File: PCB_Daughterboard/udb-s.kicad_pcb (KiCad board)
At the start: 4 copper layers, 50 x 20 mm, 10 parts, among them J1 TYPE-C-31-M-12, J2 78171-0004, U1 TPD4E05U06DQAR

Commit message: Update daughterboard 3d model
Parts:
- J2: value 78171-0004 -> 200528-0040
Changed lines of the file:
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@@
 			)
 		)
-		(property "Value" "78171-0004"
+		(property "Value" "200528-0040"
 			(at 0 5.39 0)
 			(layer "F.Fab")
@@
 			(pintype "passive")
 		)
-		(model "${KICAD8_3DMODEL_DIR}/Connector_FFC-FPC.3dshapes/Molex_200528-0040_1x04-1MP_P1.00mm_Horizontal.wrl"
+		(model "C:/Users/liuming/Desktop/PH60/PCB_Daughterboard_Model/Molex_4Pin.step"
 			(offset
-				(xyz 0 0 0)
+				(xyz 0 1 0)
 			)
 			(scale
@@
 			)
 			(rotate
-				(xyz 0 0 0)
+				(xyz 180 0 0)
 			)
 		)
@@
 			(pintype "passive")
 		)
-		(model "${PROJECT}/USB-C_Connector/USB-C_Connector.wrl"
+		(model "C:/Users/liuming/Desktop/PH60/PCB_Daughterboard_Model/USB-C.step"
 			(offset
-				(xyz 0 0 0)
+				(xyz -4.5 -3.5 0)
 			)
 			(scale
@@
 			)
 			(rotate
-				(xyz 0 0 0)
-			)
-		)
+				(xyz -90 0 0)
+			)
+		)

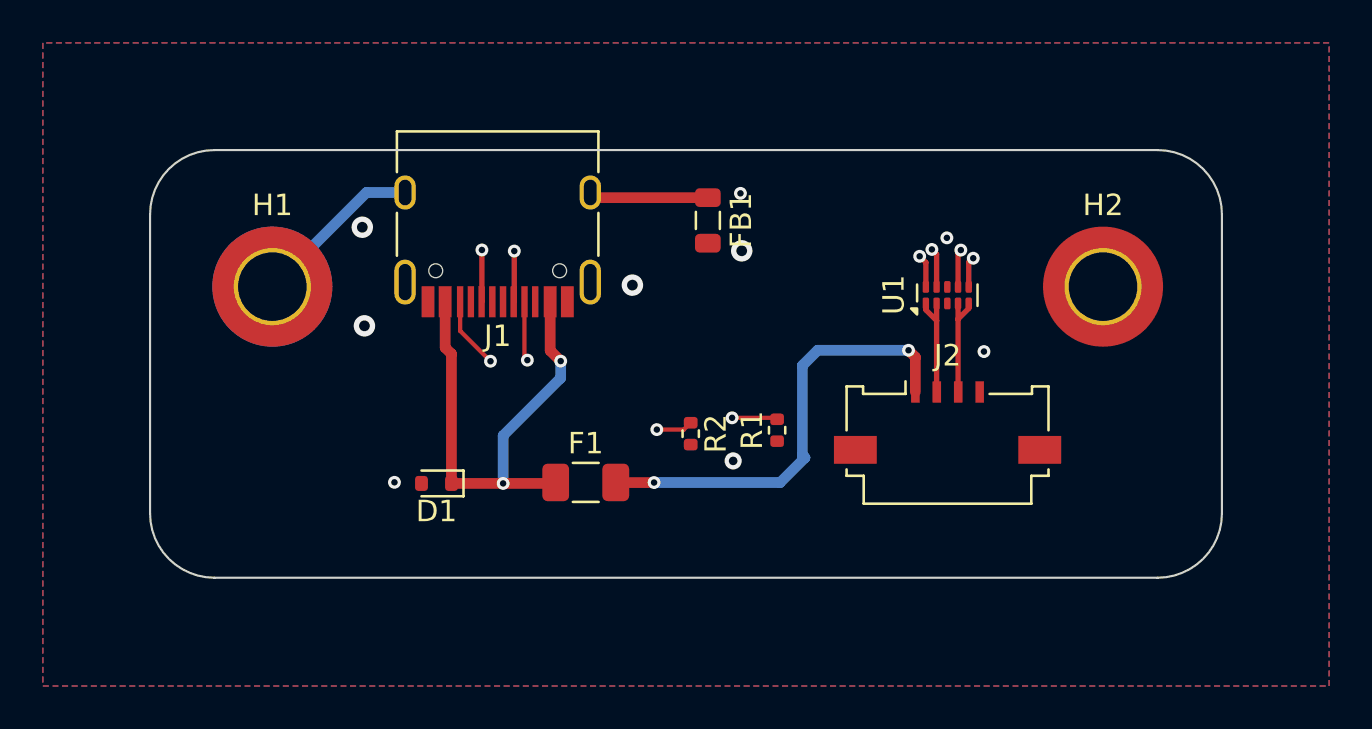
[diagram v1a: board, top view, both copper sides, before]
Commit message: Add production files
Not complete yet.
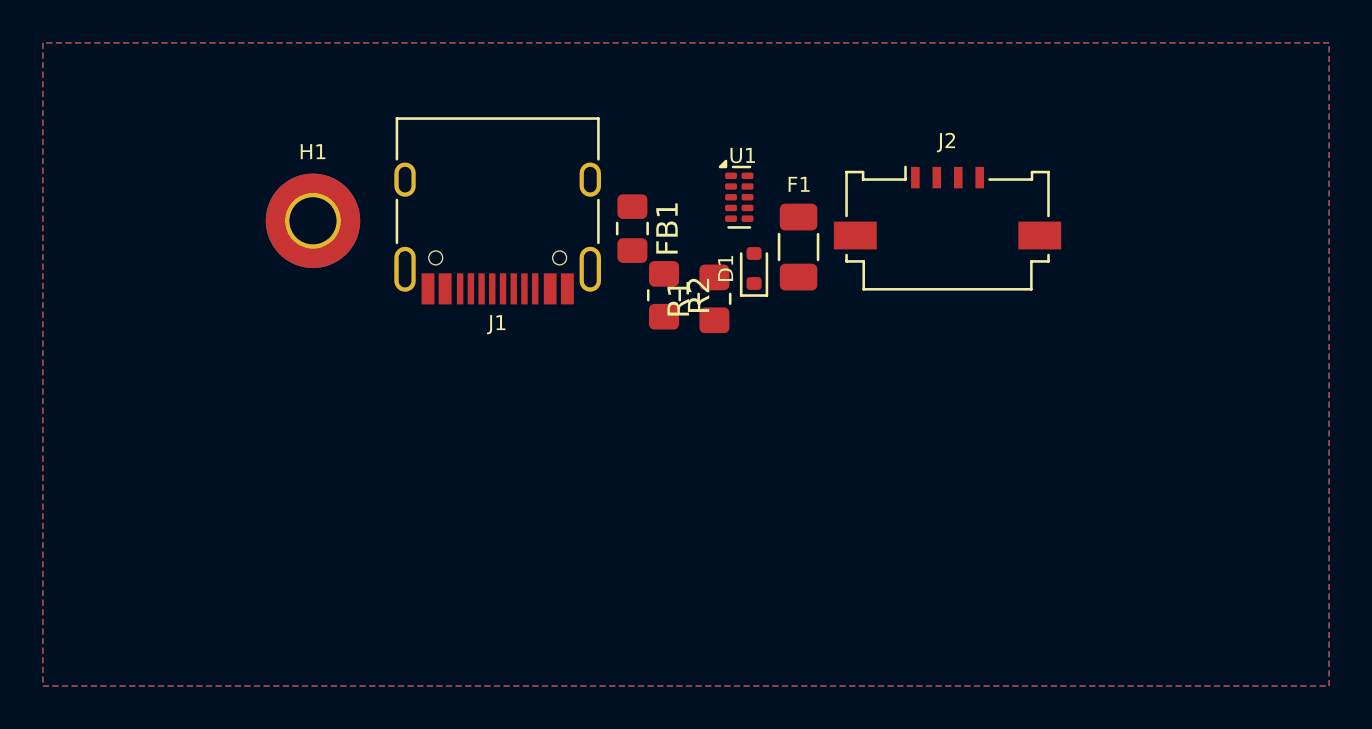
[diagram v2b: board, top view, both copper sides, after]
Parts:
- removed H2: MountingHole, MountingHole:MountingHole_3.2mm_M3_DIN965_Pad_TopOnly
- FB1: footprint Inductor_SMD:L_0805_2012Metric -> Inductor_SMD:L_0805_2012Metric_Pad1.15x1.40mm_HandSolder
- H1: footprint MountingHole:MountingHole_3.2mm_M3_DIN965_Pad_TopBottom -> MountingHole:MountingHole_2.2mm_M2_Pad_TopBottom
- R1, R2: footprint Resistor_SMD:R_0402_1005Metric -> Resistor_SMD:R_0805_2012Metric_Pad1.20x1.40mm_HandSolder
- moved D1 17.9 mm to (161.7, 37.0), turned to 90 degrees
- moved F1 14.8 mm to (163.8, 36.0), turned to 90 degrees
- moved U1 10.7 mm to (161.0, 33.7), turned to 0 degrees
- moved J2 10.0 mm to (170.7, 33.7)
- moved R1 6.79 mm to (159.8, 38.4)
- moved R2 6.57 mm to (157.5, 38.3)
- moved H1 3.61 mm to (141.1, 34.8)
- moved FB1 3.54 mm to (156.0, 35.2)
- moved J1 0.60 mm to (149.7, 33.9)
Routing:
- net D+: track 61.2 -> 0.00 mm, vias 3 -> 0
- net D-: track 52.7 -> 0.00 mm, vias 3 -> 0
- net VBUS: track 23.3 -> 0.00 mm, vias 2 -> 0
- net 5V: track 21.0 -> 0.00 mm, vias 2 -> 0
- net Net-(J1-CC1): track 15.6 -> 0.00 mm, vias 2 -> 0
- net Net-(J1-CC2): track 14.2 -> 0.00 mm, vias 2 -> 0
- net GNDPWR: track 11.3 -> 0.00 mm
- net GND: vias 8 -> 0
- net (no net): vias 1 -> 0
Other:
- board outline removed

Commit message: Add a demo daughterboard & update gerber flies
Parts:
- removed H1: MountingHole, MountingHole:MountingHole_2.2mm_M2_Pad_TopBottom
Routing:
- removed copper zone on B.Cu, net D+
- removed copper zone on F.Cu, net GND
- removed copper zone on In1.Cu, net GND
- removed copper zone on In2.Cu, net GND
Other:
- board outline added: 35 x 10 mm
